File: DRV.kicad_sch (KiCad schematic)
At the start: 34 parts, among them J1 01x03_MotorTerminal, U8 DRV8316RRGFR

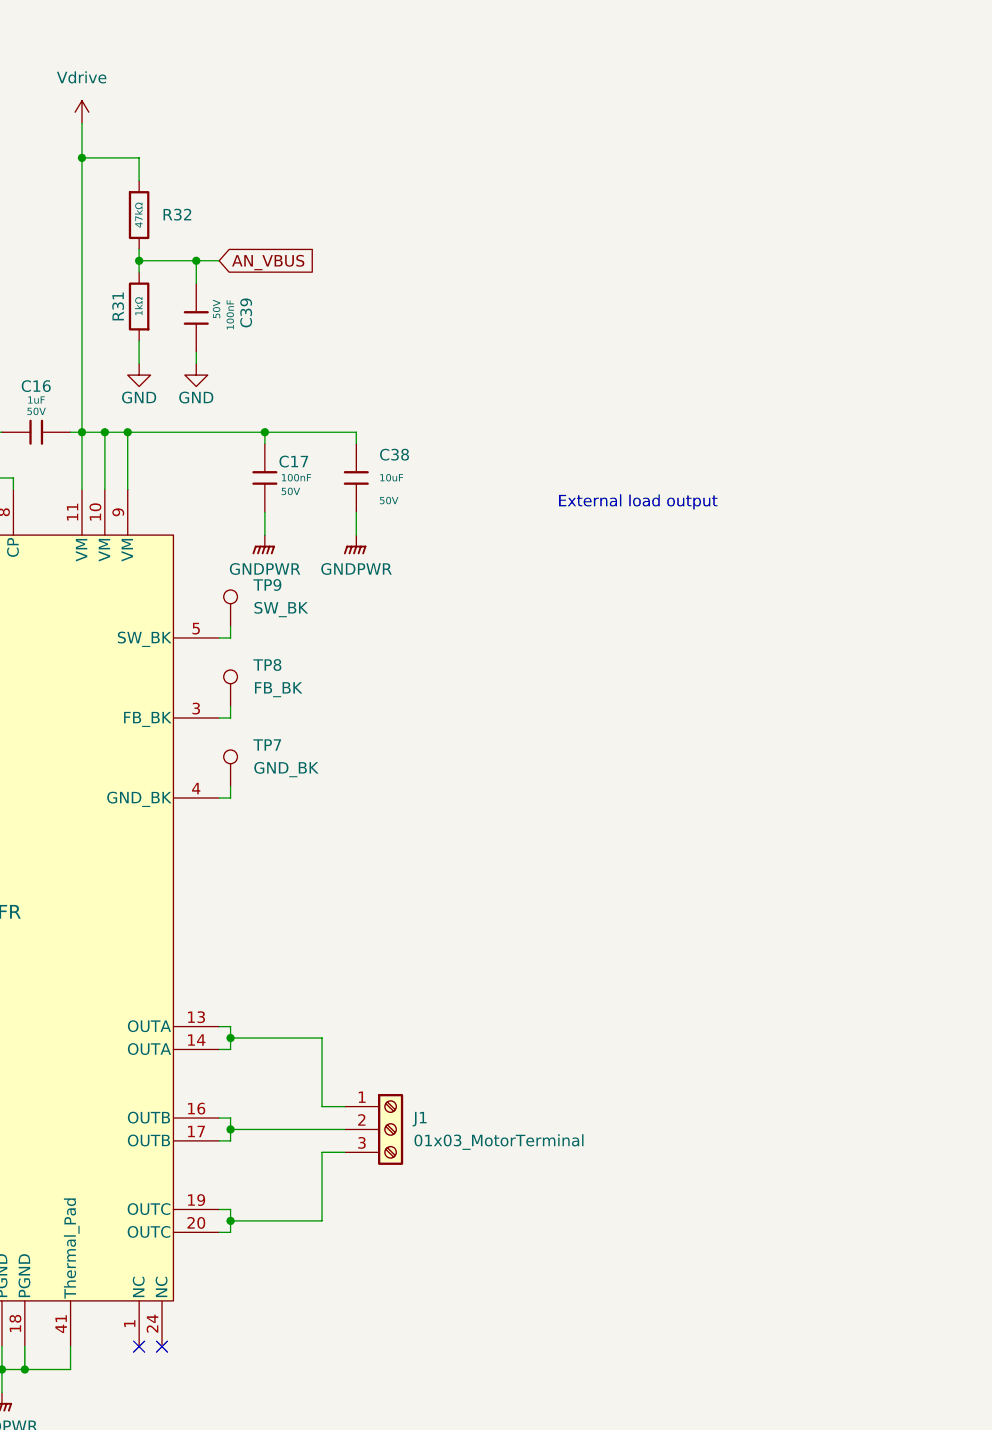
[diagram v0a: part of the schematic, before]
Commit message: Started discrete inverter version
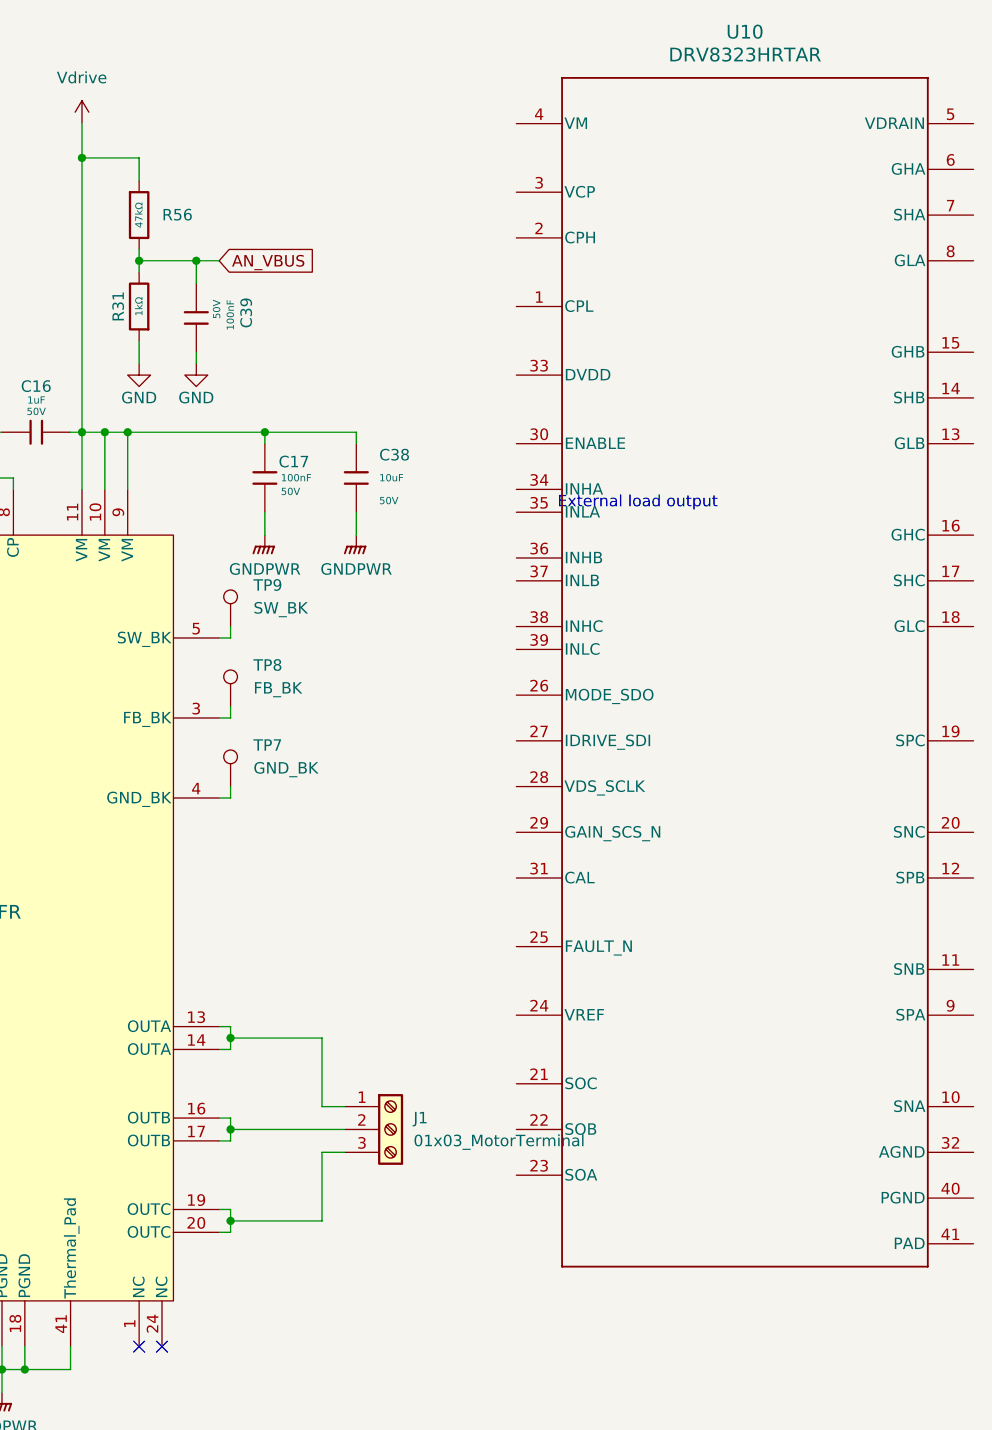
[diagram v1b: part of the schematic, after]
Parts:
- added U10: DRV8323HRTAR, RTA0040B, symbol 2026-08-10_19-21-26:DRV8323HRTAR
- renumbered R32 to R56

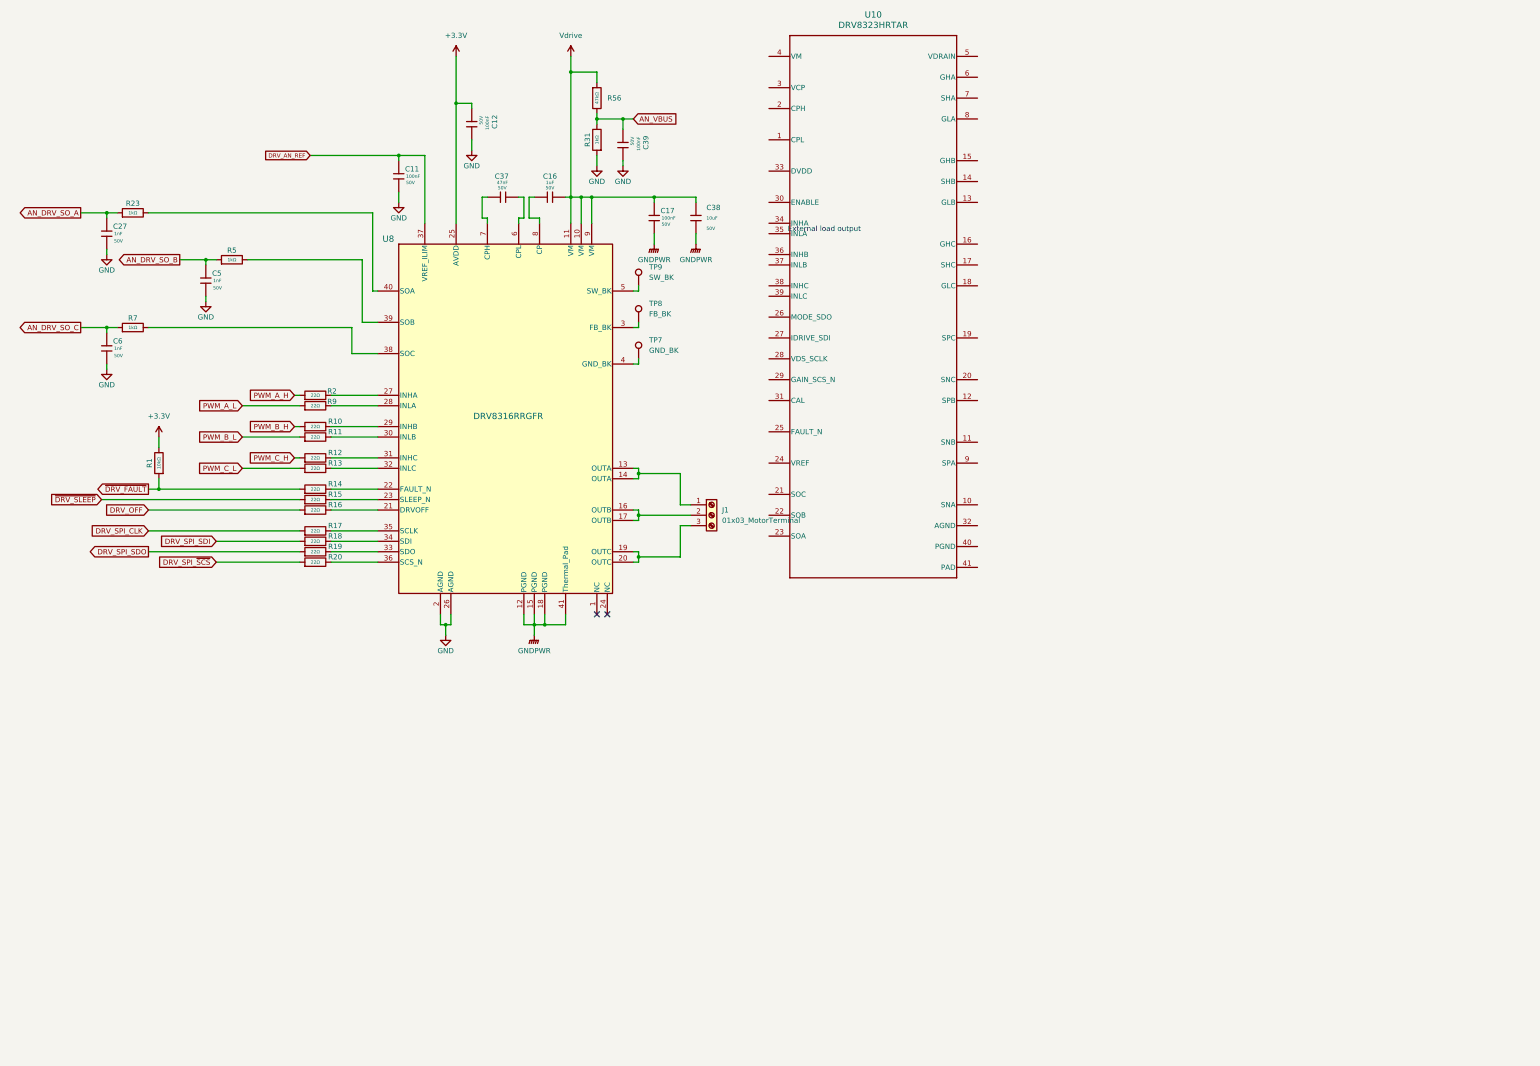
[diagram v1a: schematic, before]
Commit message: added drv8353, stm32h723vgt6
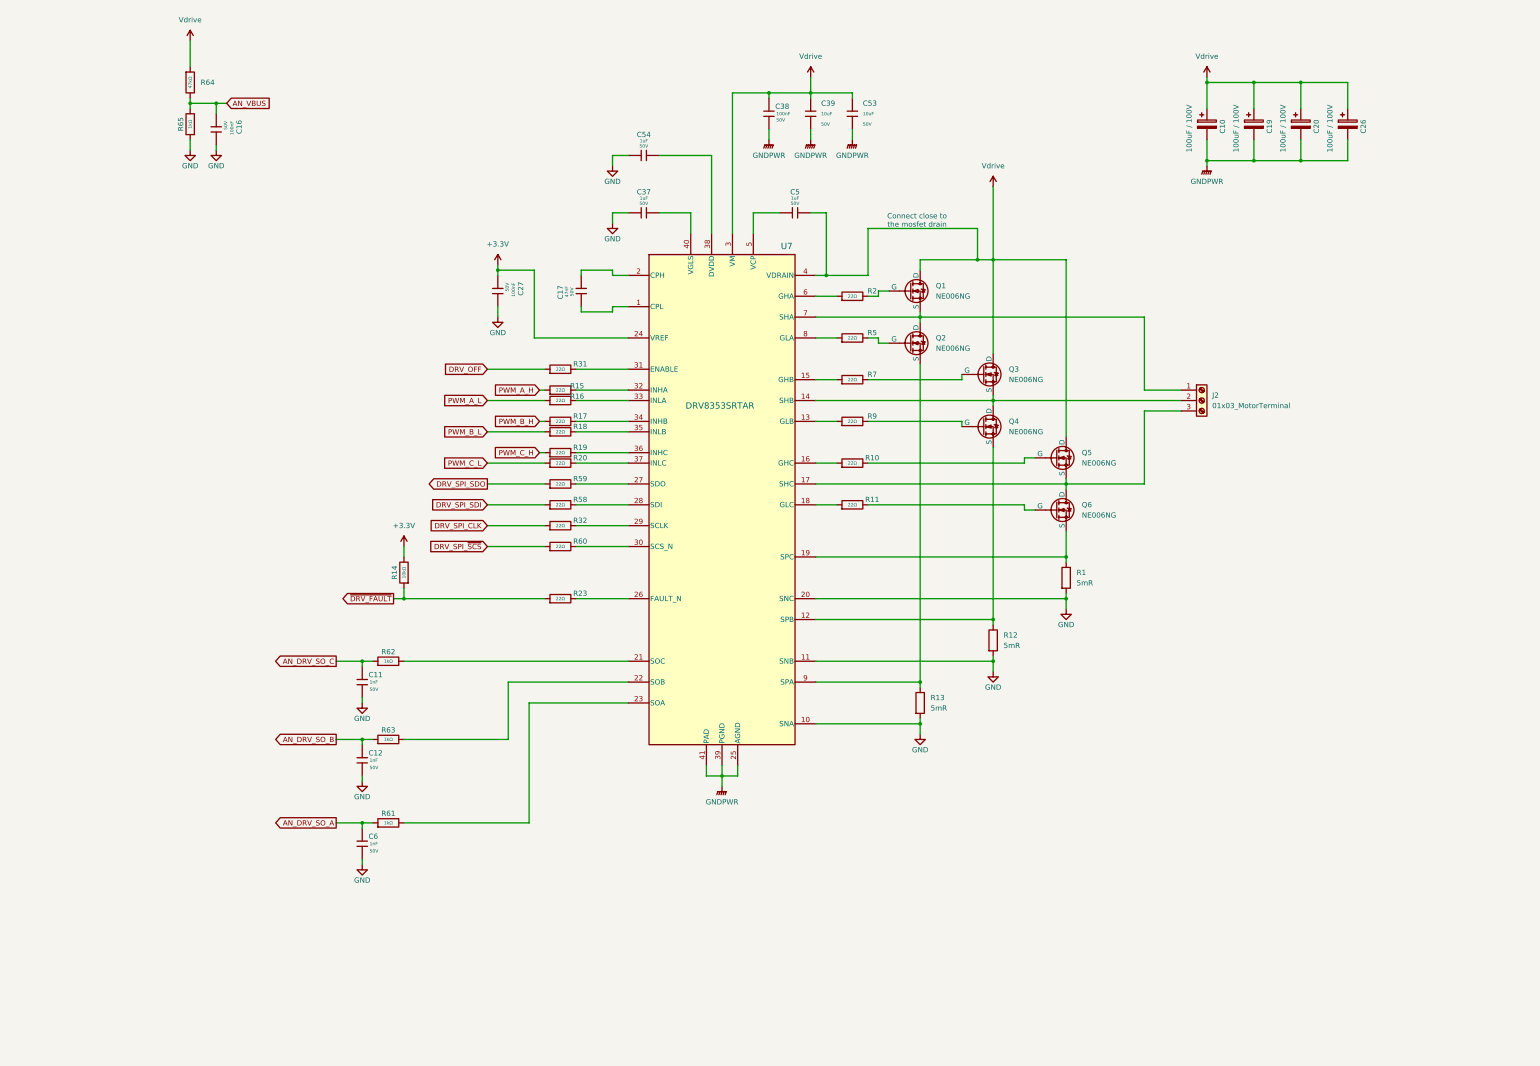
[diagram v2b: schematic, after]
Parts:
- removed C11, C12, C17, C39: 100nF, PCM_JLCPCB:C_0603, symbol PCM_JLCPCB-Capacitors:0603,100nF
- removed C16: 1uF, PCM_JLCPCB:C_0603, symbol PCM_JLCPCB-Capacitors:0603,1uF
- removed C27, C5: 1nF, PCM_JLCPCB:C_0603, symbol PCM_JLCPCB-Capacitors:0603,1nF
- removed C37: 47nF, PCM_JLCPCB:C_0603, symbol PCM_JLCPCB-Capacitors:0603,47nF
- removed C38: 10uF, PCM_JLCPCB:C_1206, symbol PCM_JLCPCB-Capacitors:1206,10uF
- removed R1: 10kΩ, PCM_JLCPCB:R_0603, symbol PCM_JLCPCB-Resistors:0603,10kΩ
- removed R12, R13, R14: 22Ω, PCM_JLCPCB:R_0603, symbol PCM_JLCPCB-Resistors:0603,22Ω
- removed R23, R31, R5, R7: 1kΩ, PCM_JLCPCB:R_0603, symbol PCM_JLCPCB-Resistors:0603,1kΩ
- removed R56: 47kΩ, PCM_JLCPCB:R_0603, symbol PCM_JLCPCB-Resistors:0603,47kΩ
- removed TP7: GND_BK, TestPoint:TestPoint_Pad_D1.0mm, symbol Connector:TestPoint
- removed TP8: FB_BK, TestPoint:TestPoint_Pad_D1.0mm, symbol Connector:TestPoint
- removed TP9: SW_BK, TestPoint:TestPoint_Pad_D1.0mm, symbol Connector:TestPoint
- removed U10: DRV8323HRTAR, RTA0040B, symbol 2026-08-10_19-21-26:DRV8323HRTAR
- removed U8: DRV8316RRGFR, DRV8316:RGF0040E-IPC_A, symbol DRV8316:DRV8316RRGFR
- added C10, C19, C20, C26: 100uF / 100V, Capacitor_SMD:CP_Elec_10x10.5, symbol Device:C_Polarized
- added C11, C12: 1nF, PCM_JLCPCB:C_0603, symbol PCM_JLCPCB-Capacitors:0603,1nF
- added C16, C27, C38: 100nF, PCM_JLCPCB:C_0603, symbol PCM_JLCPCB-Capacitors:0603,100nF
- added C17: 47nF, PCM_JLCPCB:C_0603, symbol PCM_JLCPCB-Capacitors:0603,47nF
- added C37, C5, C54: 1uF, PCM_JLCPCB:C_0603, symbol PCM_JLCPCB-Capacitors:0603,1uF
- added C39, C53: 10uF, PCM_JLCPCB:C_1206, symbol PCM_JLCPCB-Capacitors:1206,10uF
- added Q1, Q2, Q3, Q4, Q5, Q6: NE006NG, Package_DFN_QFN:AO_DFN-8-1EP_5.55x5.2mm_P1.27mm_EP4.12x4.6mm, symbol Simulation_SPICE:NMOS
- added R1, R12, R13: 5mR, Resistor_SMD:R_2512_6332Metric, symbol Device:R
- added R14: 10kΩ, PCM_JLCPCB:R_0603, symbol PCM_JLCPCB-Resistors:0603,10kΩ
- added R23, R31, R32, R5, R58, R59, R60, R7: 22Ω, PCM_JLCPCB:R_0603, symbol PCM_JLCPCB-Resistors:0603,22Ω
- added R61, R62, R63, R65: 1kΩ, PCM_JLCPCB:R_0603, symbol PCM_JLCPCB-Resistors:0603,1kΩ
- added R64: 47kΩ, PCM_JLCPCB:R_0603, symbol PCM_JLCPCB-Resistors:0603,47kΩ
- added U7: DRV8353SRTAR, RTA0040B, symbol 2026-08-11_09-32-17:DRV8353SRTAR
- renumbered J1 to J2
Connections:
- net ~{DRV_SLEEP} is gone; now on net PWM_A_H: R15.1
- net +3.3V: now also C27.1, R14.2, U7.24 (VREF)
- net AN_DRV_SO_A: now also C6.1, R61.1
- net AN_DRV_SO_B: now also C12.1, R63.1
- net AN_DRV_SO_C: now also C11.1, R62.1; no longer C6.1
- net AN_VBUS: now also C16.1, R64.2, R65.2
- net DRV_OFF: now also R31.1; no longer R16.1
- net DRV_SPI_CLK: now also R32.1; no longer R17.1
- net DRV_SPI_SDI: now also R58.1; no longer R18.1
- net DRV_SPI_SDO: now also R59.1; no longer R19.1
- net DRV_SPI_~{SCS}: now also R60.1; no longer R20.1
- net GND: now also C11.2, C12.2, C16.2, C27.2, C37.1, C54.1, R1.2, R12.2, R13.2, R65.1, U7.10 (SNA), U7.11 (SNB), U7.20 (SNC)
- net GNDPWR: now also C10.2, C19.2, C20.2, C26.2, C38.2, C39.2, C53.2, U7.25 (AGND), U7.39 (PGND), U7.41 (PAD)
- net PWM_A_H: no longer R2.1
- net PWM_A_L: now also R16.1; no longer R9.1
- net PWM_B_H: now also R17.1; no longer R10.1
- net PWM_B_L: now also R18.1; no longer R11.1
- net PWM_C_H: now also R19.1
- net PWM_C_L: now also R20.1
- net Vdrive: now also C10.1, C19.1, C20.1, C26.1, C38.1, C39.1, C5.2, C53.1, Q1.3 (D), Q3.3 (D), Q5.3 (D), R64.1, U7.3 (VM), U7.4 (VDRAIN)
- net ~{DRV_FAULT}: now also R14.1, R23.1
- net at R16.2: now also U7.33 (INLA)
- net at R18.2: now also U7.35 (INLB)
- net at R11.2: now also Q6.1 (G)
- net at J2.1 (Pin_1): now also Q1.2 (S), Q2.3 (D), U7.7 (SHA)
- net at J2.2 (Pin_2): now also Q3.2 (S), Q4.3 (D), U7.14 (SHB)
- net at J2.3 (Pin_3): now also Q5.2 (S), Q6.3 (D), U7.17 (SHC)
- net at R15.2: now also U7.32 (INHA)
- net at R2.2: now also Q1.1 (G)
- net at R9.2: now also Q4.1 (G)
- net at R10.2: now also Q5.1 (G)
- net at R19.2: now also U7.36 (INHC)
- net at R17.2: now also U7.34 (INHB)
- net at R20.2: now also U7.37 (INLC)
- new net: R58.2, U7.28 (SDI)
- new net: R23.2, U7.26 (FAULT_N)
- new net: Q2.1 (G), R5.2
- new net: Q2.2 (S), R13.1, U7.9 (SPA)
- new net: R11.1, U7.18 (GLC)
- new net: C37.2, U7.40 (VGLS)
- new net: R62.2, U7.21 (SOC)
- new net: R31.2, U7.31 (ENABLE)
- new net: Q6.2 (S), R1.1, U7.19 (SPC)
- new net: R7.1, U7.15 (GHB)
- new net: Q3.1 (G), R7.2
- new net: C54.2, U7.38 (DVDD)
- new net: C17.1, U7.1 (CPL)
- new net: C17.2, U7.2 (CPH)
- new net: R10.1, U7.16 (GHC)
- new net: R9.1, U7.13 (GLB)
- new net: R2.1, U7.6 (GHA)
- new net: R60.2, U7.30 (SCS_N)
- new net: Q4.2 (S), R12.1, U7.12 (SPB)
- new net: R63.2, U7.22 (SOB)
- new net: R61.2, U7.23 (SOA)
- new net: R59.2, U7.27 (SDO)
- new net: R32.2, U7.29 (SCLK)
- new net: C5.1, U7.5 (VCP)
- new net: R5.1, U7.8 (GLA)
- no-connect marks 2 -> 0
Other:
- note added: "Connect close to the mosfet drain"
- note removed: "External load output"
- moved on the sheet: J2
